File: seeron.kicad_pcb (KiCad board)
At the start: 2 copper layers, 25.4 x 25.4 mm, 13 parts

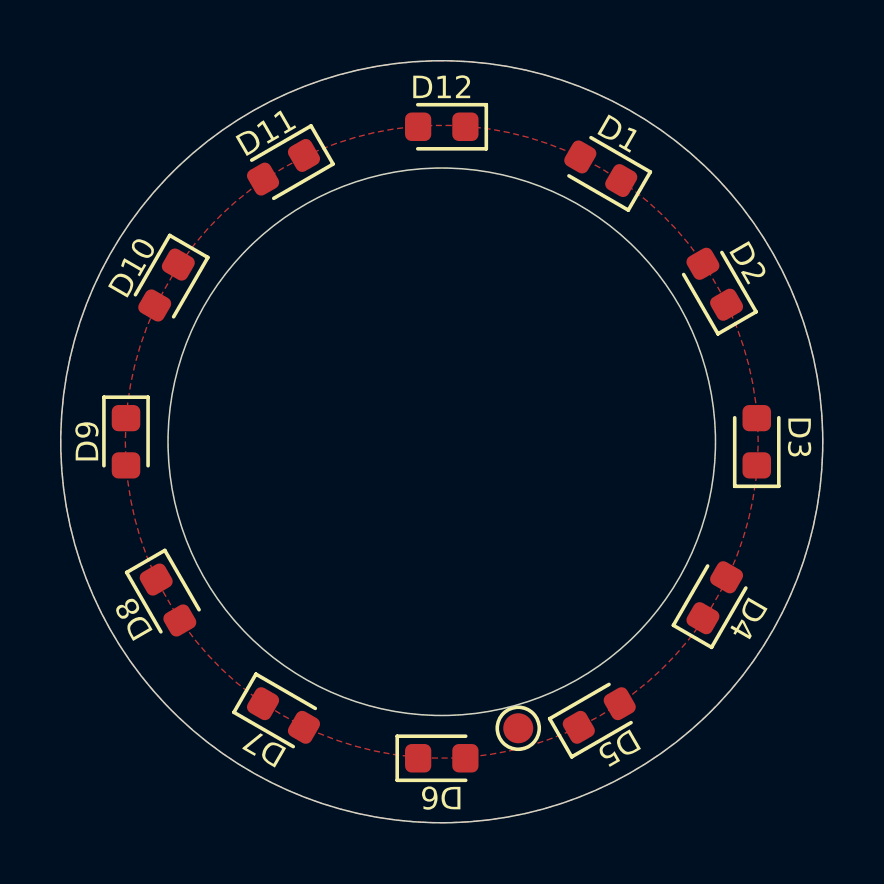
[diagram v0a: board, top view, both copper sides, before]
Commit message: Add readme and more test points for providing power contacts if solder mask is used
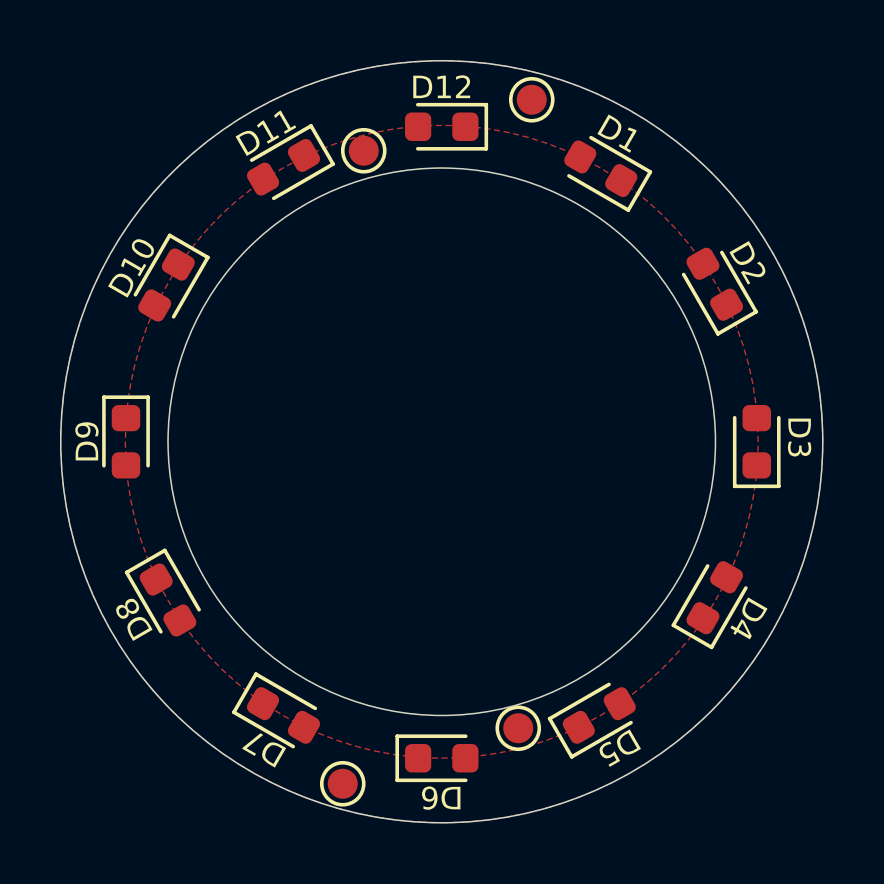
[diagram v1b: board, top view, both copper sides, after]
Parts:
- added TP2: 3v3, TestPoint:TestPoint_Pad_D1.0mm, F.Cu at (127.4, 90.3)
- added TP3: GND, TestPoint:TestPoint_Pad_D1.0mm, F.Cu at (133.0, 88.6)
- added TP4: GND, TestPoint:TestPoint_Pad_D1.0mm, F.Cu at (126.7, 111.4)
- TP1: value TestPoint -> 3v3
